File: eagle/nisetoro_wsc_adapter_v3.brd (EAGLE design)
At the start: 72 x 48.5 mm, 29 parts, among them CN3 WSC LCD, Q1 MMBT2222A, Q2 MMBT2222A, U2 24LC00ST, U3 TLV1117-15

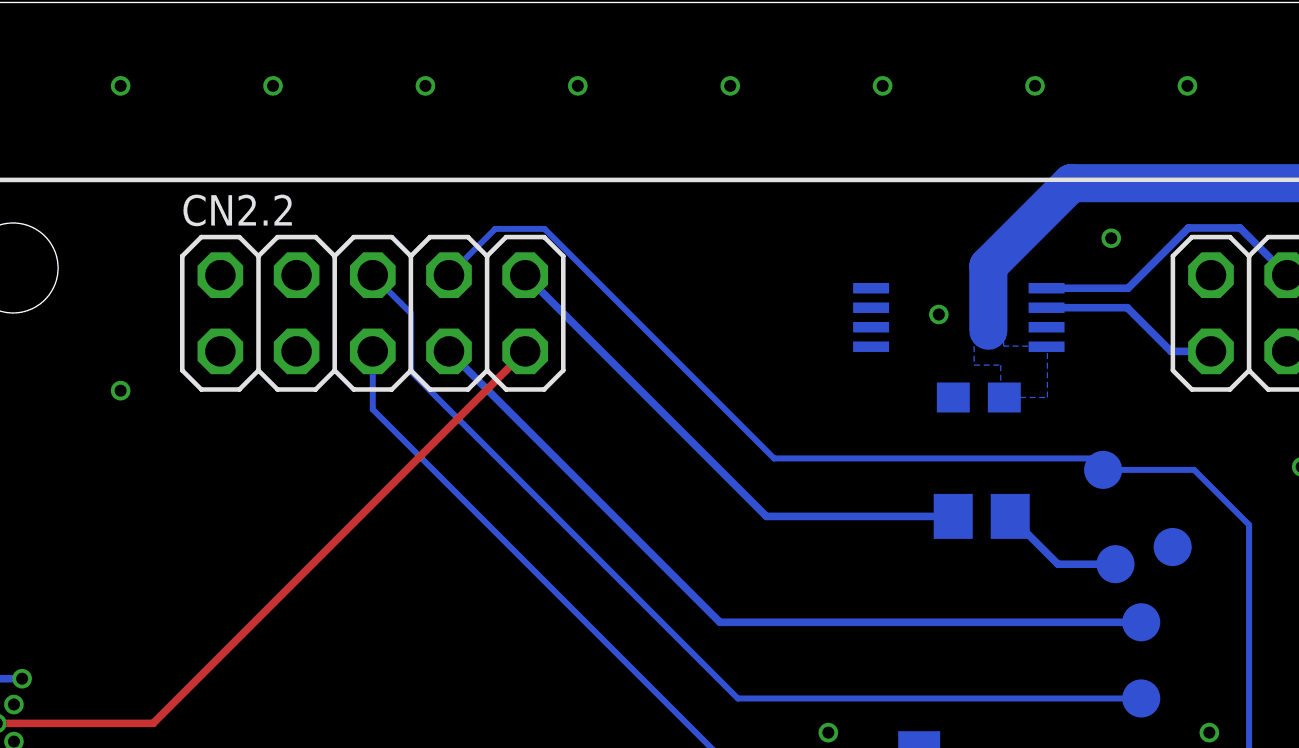
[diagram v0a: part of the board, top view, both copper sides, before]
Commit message: EAGLE: Update adapter PCB to V3c
PREVIEW: Fix sound icon

MAX2: Set audio reg default value to 1 to match new version PCB
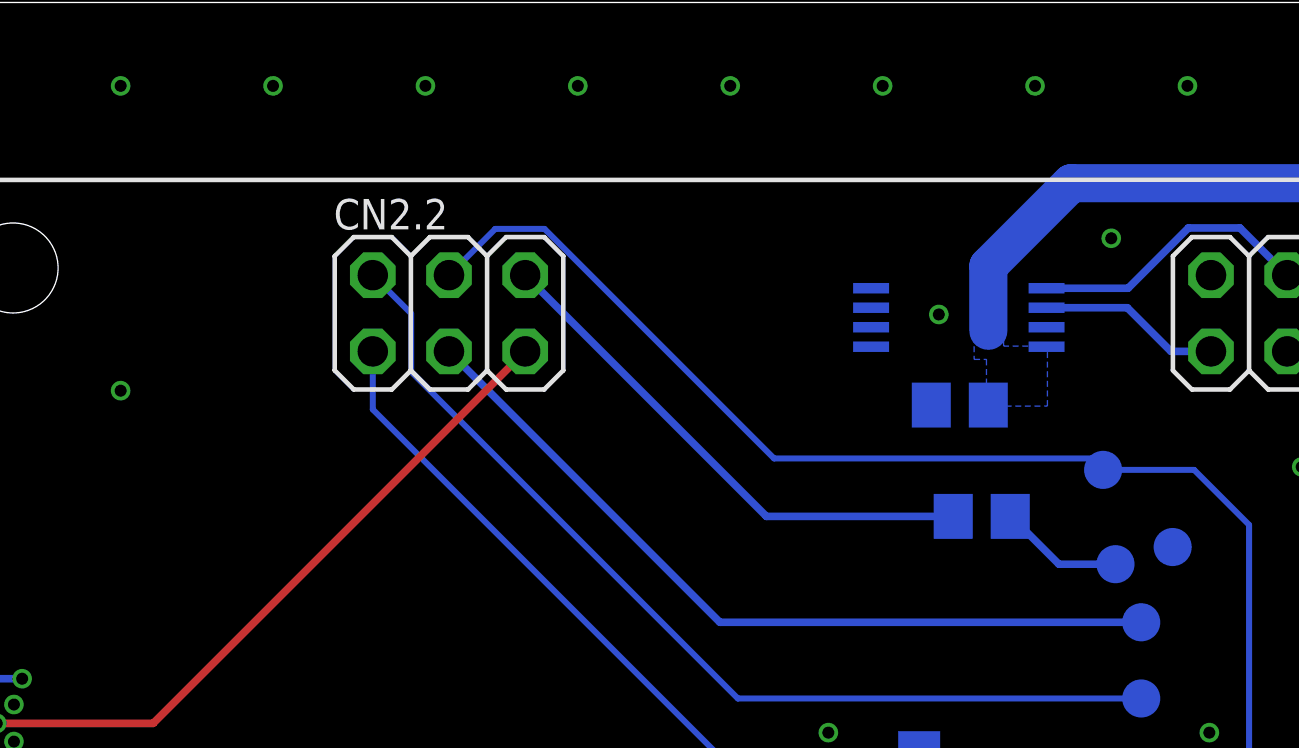
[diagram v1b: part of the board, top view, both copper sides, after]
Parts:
- C1: device rcl:C0603 -> rcl:C0805
- CN2.2: device pinhead:2X05 -> pinhead:2X03
- R5: value 470 -> 330
- moved CN2.2 2.54 mm to (24.9, 38.1)
- moved C1 0.68 mm to (41.9, 35.1)
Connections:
- removed net IO70: CN2.2.8
- removed net IO71: CN2.2.7
- removed net IO72: CN2.2.10
- removed net IO73: CN2.2.9
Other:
- board text added: "Designed by splash5"
- board text added: "NISETORO WSC ADAPTER V3c"
- board text removed: "NISETORO WSC ADAPTER V3b"
